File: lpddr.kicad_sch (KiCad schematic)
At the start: 3 parts

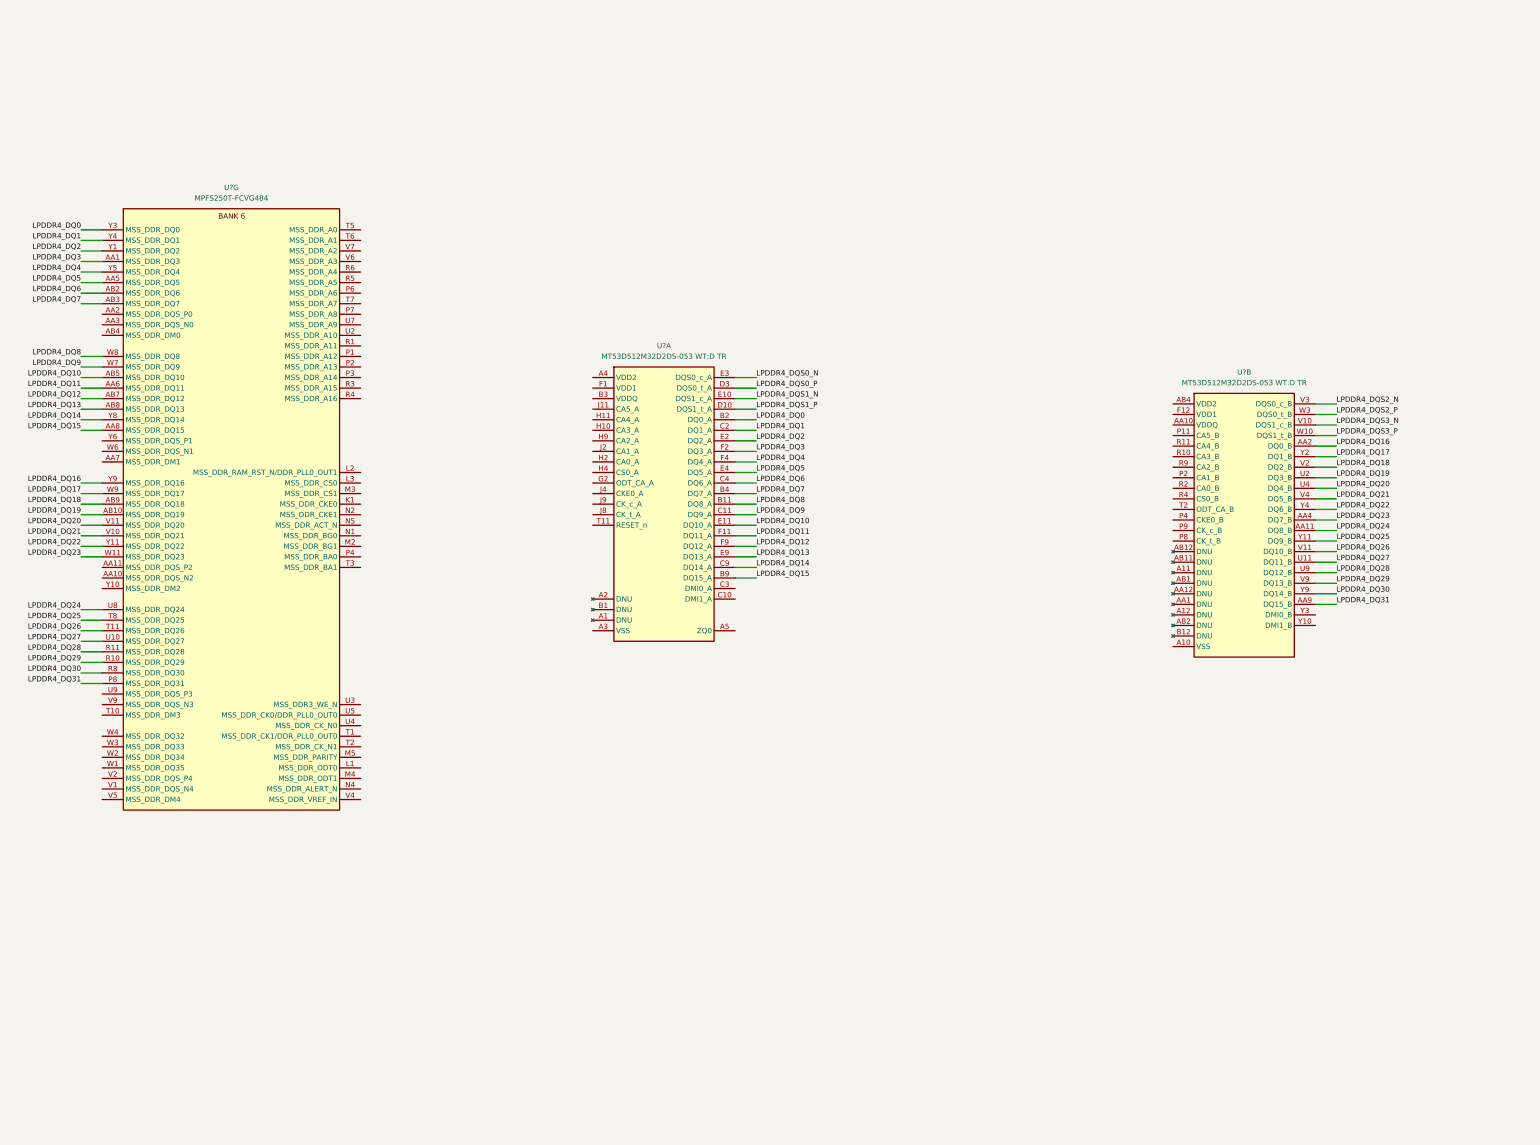
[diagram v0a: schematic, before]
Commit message: [#52579] Connect signals to SoC
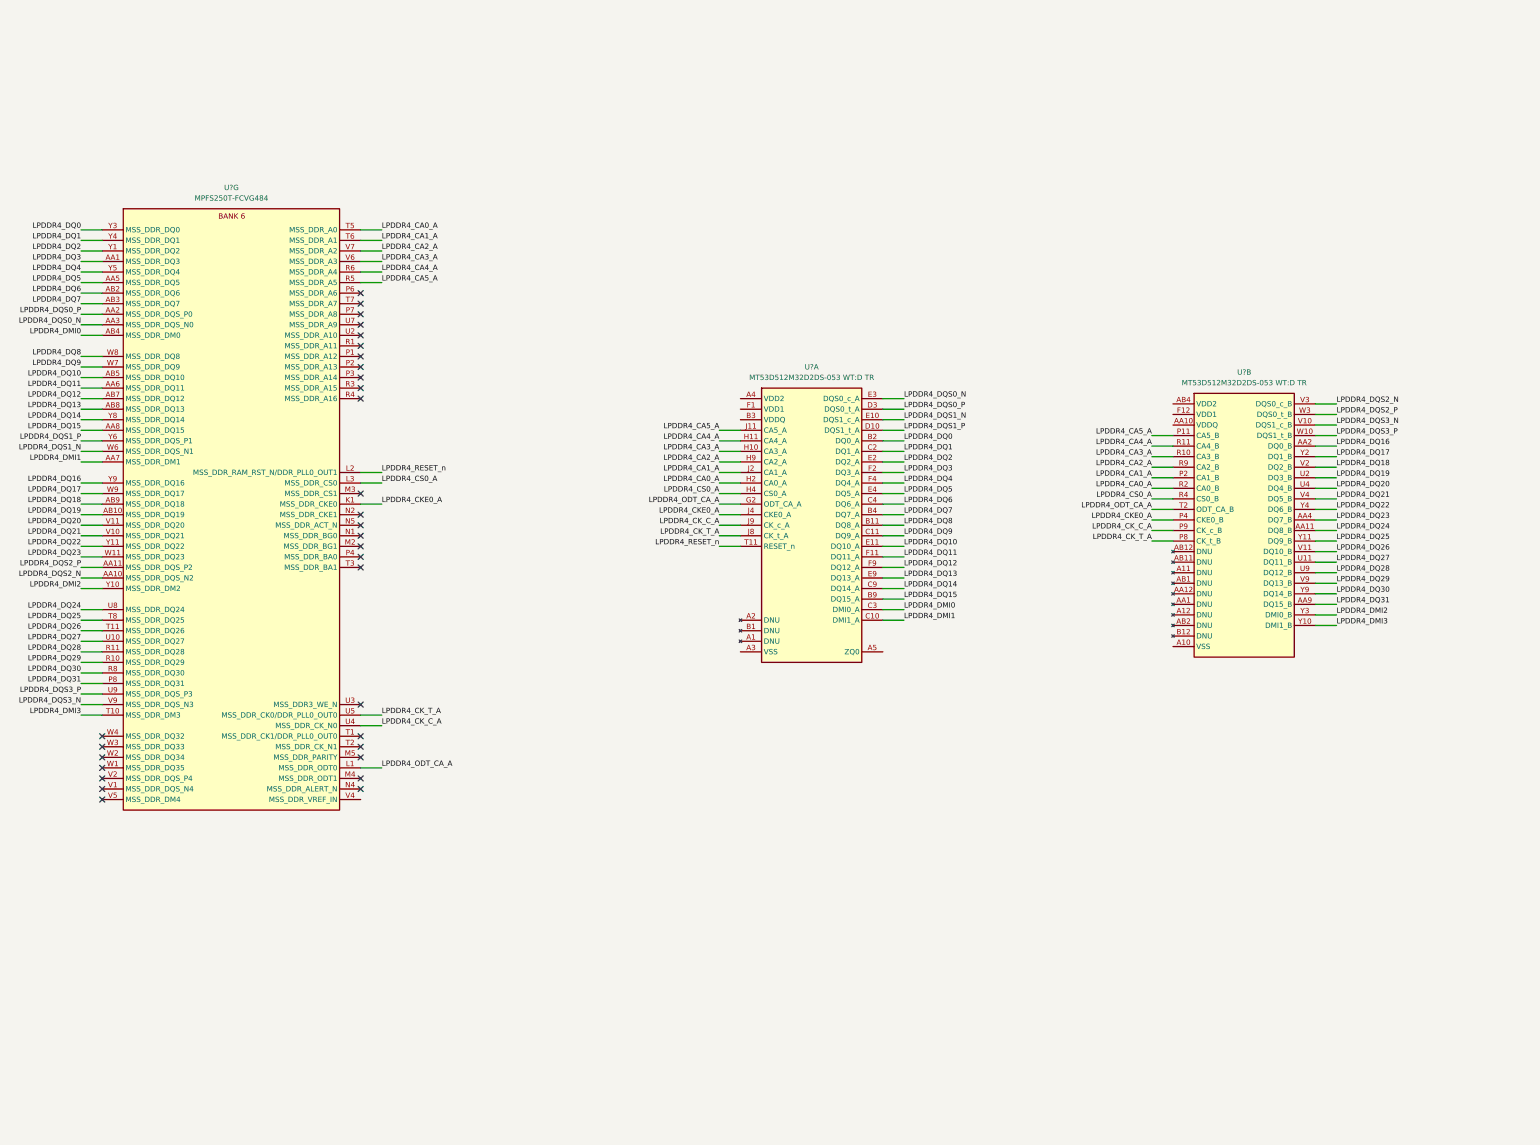
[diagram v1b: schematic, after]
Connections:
- net LPDDR4_DQS0_N: now also U?.AA3 (MSS_DDR_DQS_N0)
- net LPDDR4_DQS0_P: now also U?.AA2 (MSS_DDR_DQS_P0)
- net LPDDR4_DQS1_N: now also U?.W6 (MSS_DDR_DQS_N1)
- net LPDDR4_DQS1_P: now also U?.Y6 (MSS_DDR_DQS_P1)
- net LPDDR4_DQS2_N: now also U?.AA10 (MSS_DDR_DQS_N2)
- net LPDDR4_DQS2_P: now also U?.AA11 (MSS_DDR_DQS_P2)
- net LPDDR4_DQS3_N: now also U?.V9 (MSS_DDR_DQS_N3)
- net LPDDR4_DQS3_P: now also U?.U9 (MSS_DDR_DQS_P3)
- net LPDDR4_CA5_A: now reaches U?.P11 (CA5_B)
- net LPDDR4_CA5_A: now also U?.J11 (CA5_A), U?.R5 (MSS_DDR_A5)
- net LPDDR4_CA1_A: now reaches U?.P2 (CA1_B)
- net LPDDR4_CA1_A: now also U?.J2 (CA1_A), U?.T6 (MSS_DDR_A1)
- net LPDDR4_CKE0_A: now reaches U?.P4 (CKE0_B)
- net LPDDR4_CKE0_A: now also U?.J4 (CKE0_A), U?.K1 (MSS_DDR_CKE0)
- net LPDDR4_CK_T_A: now reaches U?.P8 (CK_t_B)
- net LPDDR4_CK_T_A: now also U?.J8 (CK_t_A), U?.U5 (MSS_DDR_CK0/DDR_PLL0_OUT0)
- net LPDDR4_CK_C_A: now reaches U?.P9 (CK_c_B)
- net LPDDR4_CK_C_A: now also U?.J9 (CK_c_A), U?.U4 (MSS_DDR_CK_N0)
- net LPDDR4_CA3_A: now reaches U?.R10 (CA3_B)
- net LPDDR4_CA3_A: now also U?.H10 (CA3_A), U?.V6 (MSS_DDR_A3)
- net LPDDR4_CA4_A: now reaches U?.R11 (CA4_B)
- net LPDDR4_CA4_A: now also U?.H11 (CA4_A), U?.R6 (MSS_DDR_A4)
- net LPDDR4_CA0_A: now reaches U?.R2 (CA0_B)
- net LPDDR4_CA0_A: now also U?.H2 (CA0_A), U?.T5 (MSS_DDR_A0)
- net LPDDR4_CS0_A: now reaches U?.R4 (CS0_B)
- net LPDDR4_CS0_A: now also U?.H4 (CS0_A), U?.L3 (MSS_DDR_CS0)
- net LPDDR4_CA2_A: now reaches U?.R9 (CA2_B)
- net LPDDR4_CA2_A: now also U?.H9 (CA2_A), U?.V7 (MSS_DDR_A2)
- net LPDDR4_ODT_CA_A: now reaches U?.T2 (ODT_CA_B)
- net LPDDR4_ODT_CA_A: now also U?.G2 (ODT_CA_A), U?.L1 (MSS_DDR_ODT0)
- net LPDDR4_DMI3: now reaches U?.Y10 (DMI1_B)
- net LPDDR4_DMI3: now also U?.T10 (MSS_DDR_DM3)
- net LPDDR4_DMI2: now reaches U?.Y3 (DMI0_B)
- net LPDDR4_DMI2: now also U?.Y10 (MSS_DDR_DM2)
- net LPDDR4_DMI1: now reaches U?.AA7 (MSS_DDR_DM1)
- net LPDDR4_DMI1: now also U?.C10 (DMI1_A)
- net LPDDR4_DMI0: now reaches U?.AB4 (MSS_DDR_DM0)
- net LPDDR4_DMI0: now also U?.C3 (DMI0_A)
- net LPDDR4_RESET_n: now reaches U?.L2 (MSS_DDR_RAM_RST_N/DDR_PLL0_OUT1)
- net LPDDR4_RESET_n: now also U?.T11 (RESET_n)
- no-connect marks 0 -> 31
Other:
- moved on the sheet: U?A

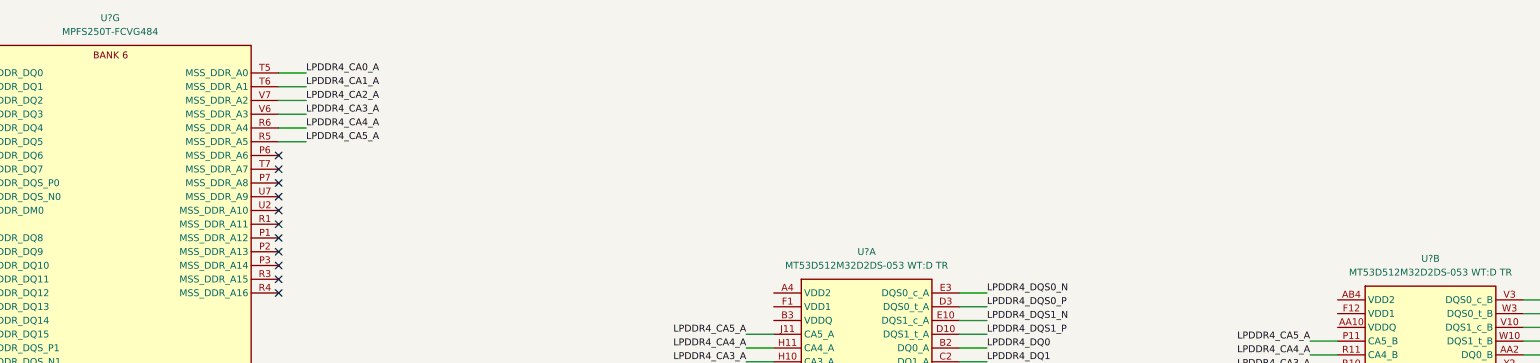
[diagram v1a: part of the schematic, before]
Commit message: [#52579] Connect CSI and DSI to CrossLink
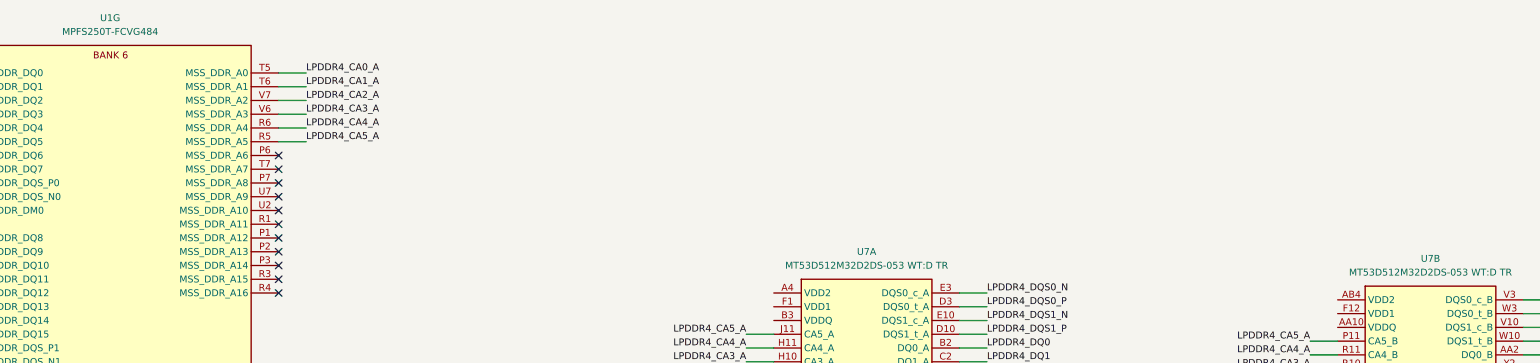
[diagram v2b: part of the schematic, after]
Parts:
- gave numbers to parts that had none: 2
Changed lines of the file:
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@@
   (symbol (lib_id "antmicroMemory:MT53D512M32D2_WFBGA") (at 321.31 107.95 0) (unit 2)
     (in_bom yes) (on_board yes) (fields_autoplaced)
-    (property "Reference" "U?" (id 0) (at 338.455 100.33 0)
+    (property "Reference" "U7" (id 0) (at 338.455 100.33 0)
       (effects (font (size 1.27 1.27) (thickness 0.15)))
     )
@@
   (symbol (lib_id "antmicroMicrocontrollers:MPFS250T-FCVG484") (at 63.5 66.04 0) (unit 7)
     (in_bom yes) (on_board yes) (fields_autoplaced)
-    (property "Reference" "U?" (id 0) (at 94.615 55.88 0)
+    (property "Reference" "U1" (id 0) (at 94.615 55.88 0)
       (effects (font (size 1.27 1.27) (thickness 0.15)))
     )
@@
   (symbol (lib_id "antmicroMemory:MT53D512M32D2_WFBGA") (at 217.17 106.68 0) (unit 1)
     (in_bom yes) (on_board yes) (fields_autoplaced)
-    (property "Reference" "U?" (id 0) (at 234.315 99.06 0)
+    (property "Reference" "U7" (id 0) (at 234.315 99.06 0)
       (effects (font (size 1.27 1.27) (thickness 0.15)))
     )

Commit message: [#52577] Clear annotations
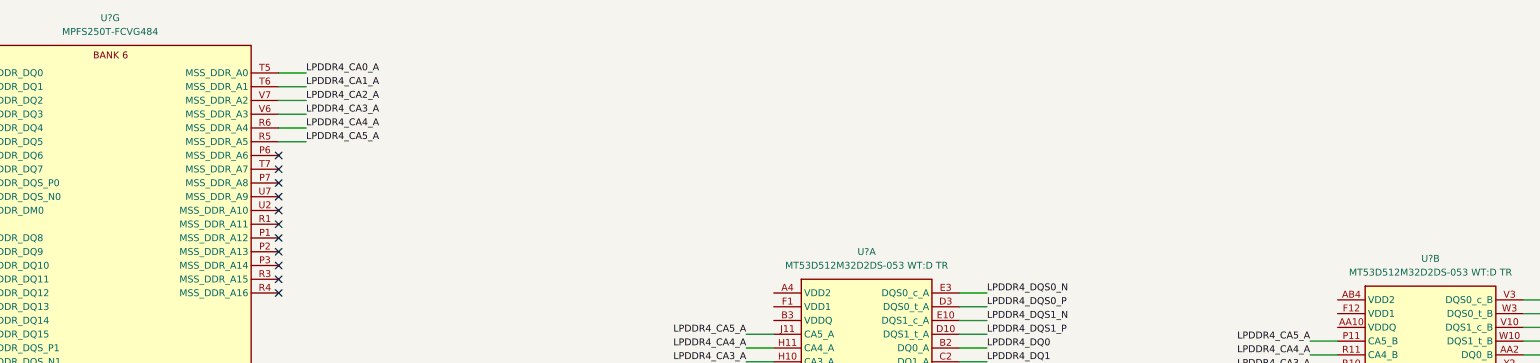
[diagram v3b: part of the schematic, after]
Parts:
- renumbered U7 to U?, U1 to U?
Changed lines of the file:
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@@
   (symbol (lib_id "antmicroMemory:MT53D512M32D2_WFBGA") (at 321.31 107.95 0) (unit 2)
     (in_bom yes) (on_board yes) (fields_autoplaced)
-    (property "Reference" "U7" (id 0) (at 338.455 100.33 0)
+    (property "Reference" "U?" (id 0) (at 338.455 100.33 0)
       (effects (font (size 1.27 1.27) (thickness 0.15)))
     )
@@
   (symbol (lib_id "antmicroMicrocontrollers:MPFS250T-FCVG484") (at 63.5 66.04 0) (unit 7)
     (in_bom yes) (on_board yes) (fields_autoplaced)
-    (property "Reference" "U1" (id 0) (at 94.615 55.88 0)
+    (property "Reference" "U?" (id 0) (at 94.615 55.88 0)
       (effects (font (size 1.27 1.27) (thickness 0.15)))
     )
@@
   (symbol (lib_id "antmicroMemory:MT53D512M32D2_WFBGA") (at 217.17 106.68 0) (unit 1)
     (in_bom yes) (on_board yes) (fields_autoplaced)
-    (property "Reference" "U7" (id 0) (at 234.315 99.06 0)
+    (property "Reference" "U?" (id 0) (at 234.315 99.06 0)
       (effects (font (size 1.27 1.27) (thickness 0.15)))
     )

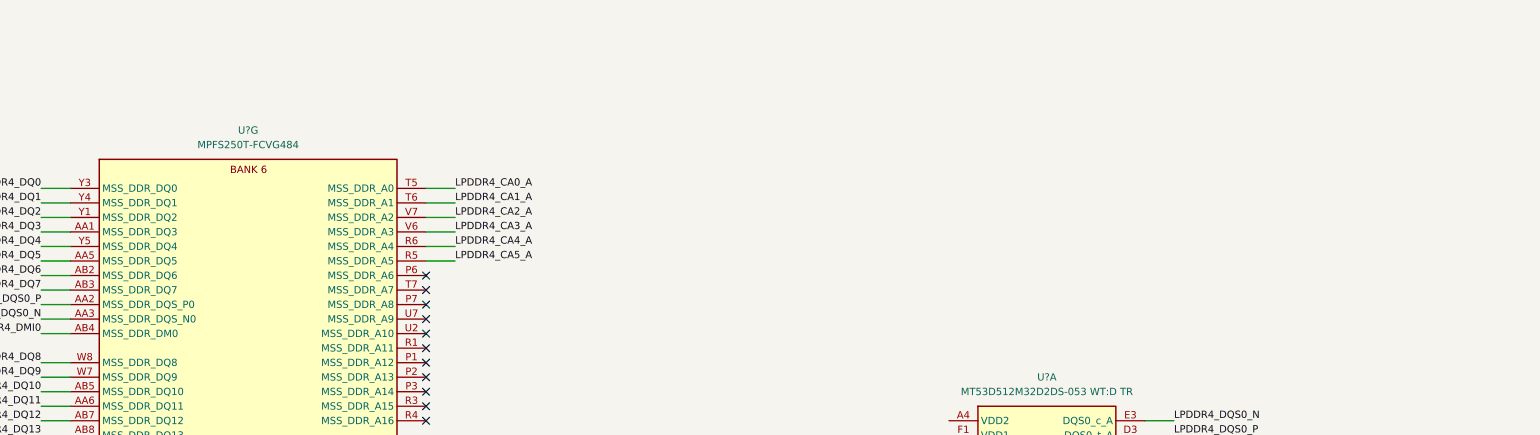
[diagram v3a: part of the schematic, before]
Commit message: [#54084] Sheets cleanup
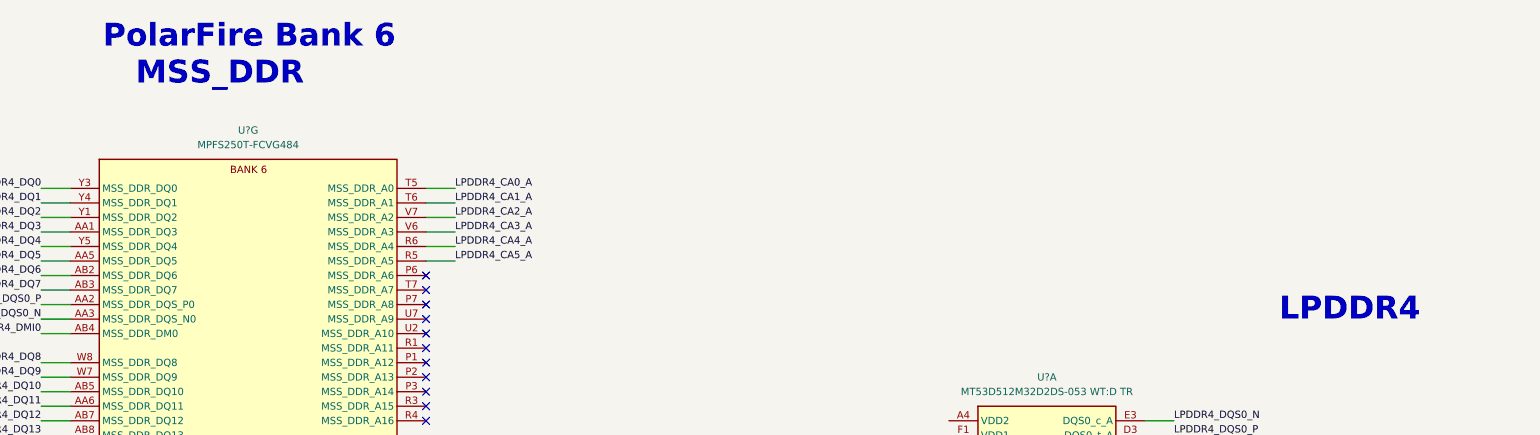
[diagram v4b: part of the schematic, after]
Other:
- note added: "LPDDR4"
- note added: "PolarFire Bank 6 MSS_DDR"
- company: (none) -> Antmicro Ltd
- title: (none) -> PolarFire SoM

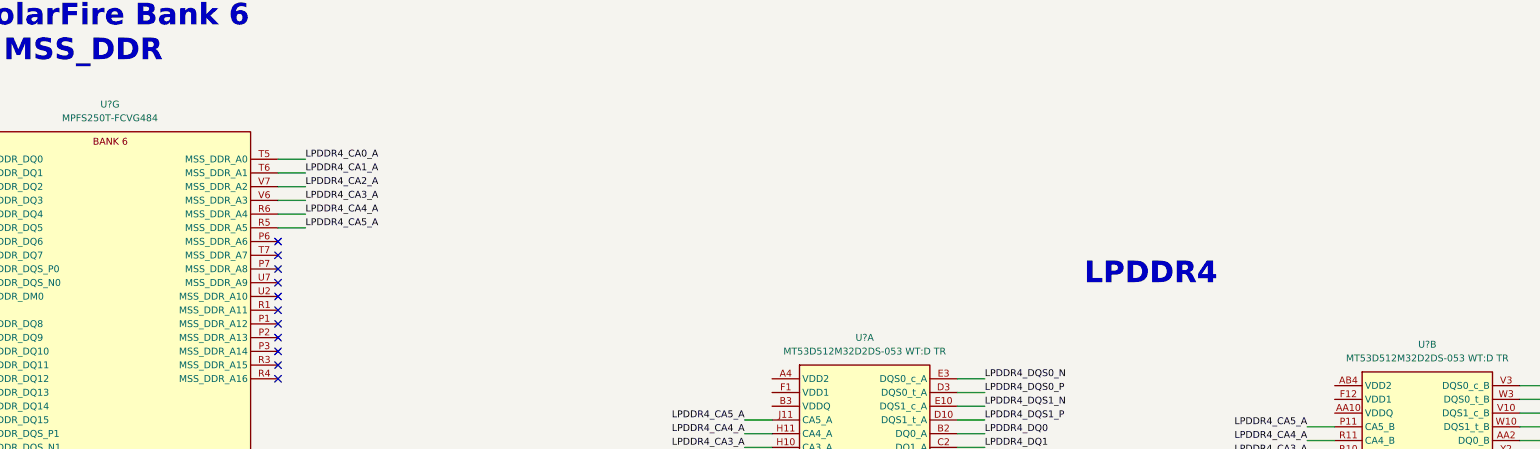
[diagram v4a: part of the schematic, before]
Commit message: [#54016] Place components to assess available space
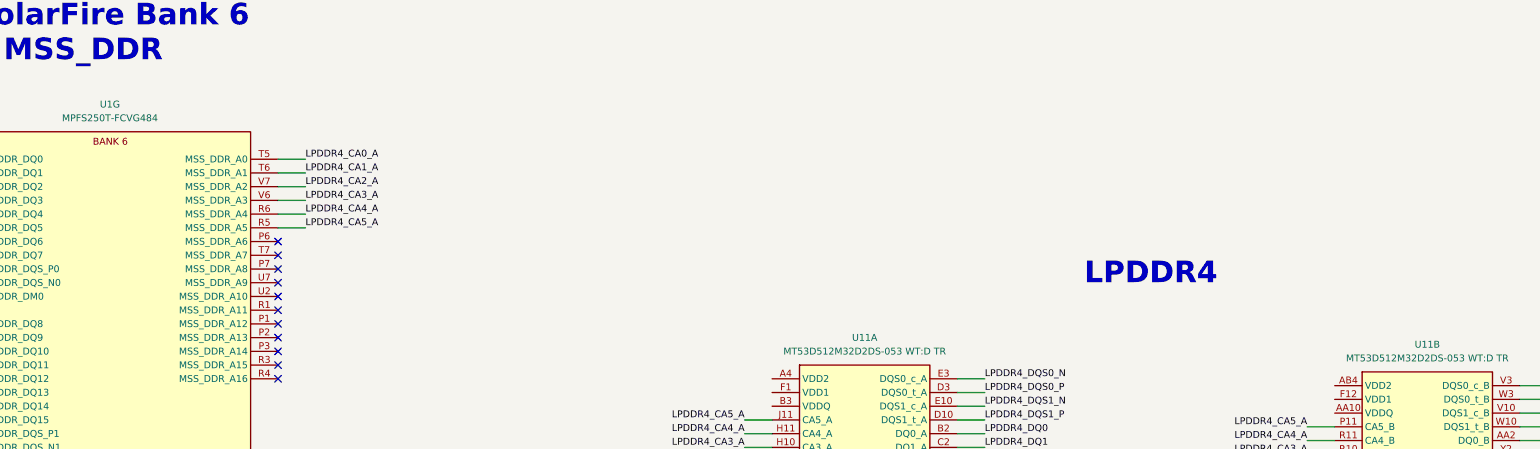
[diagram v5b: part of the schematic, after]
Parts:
- gave numbers to parts that had none: 2
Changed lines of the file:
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@@
   (symbol (lib_id "antmicroMemory:MT53D512M32D2_WFBGA") (at 321.31 107.95 0) (unit 2)
     (in_bom yes) (on_board yes) (fields_autoplaced)
-    (property "Reference" "U?" (id 0) (at 338.455 100.33 0)
+    (property "Reference" "U11" (id 0) (at 338.455 100.33 0)
       (effects (font (size 1.27 1.27) (thickness 0.15)))
     )
@@
   (symbol (lib_id "antmicroMicrocontrollers:MPFS250T-FCVG484") (at 63.5 66.04 0) (unit 7)
     (in_bom yes) (on_board yes) (fields_autoplaced)
-    (property "Reference" "U?" (id 0) (at 94.615 55.88 0)
+    (property "Reference" "U1" (id 0) (at 94.615 55.88 0)
       (effects (font (size 1.27 1.27) (thickness 0.15)))
     )
@@
   (symbol (lib_id "antmicroMemory:MT53D512M32D2_WFBGA") (at 217.17 106.68 0) (unit 1)
     (in_bom yes) (on_board yes) (fields_autoplaced)
-    (property "Reference" "U?" (id 0) (at 234.315 99.06 0)
+    (property "Reference" "U11" (id 0) (at 234.315 99.06 0)
       (effects (font (size 1.27 1.27) (thickness 0.15)))
     )
